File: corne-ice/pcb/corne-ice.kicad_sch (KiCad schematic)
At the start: 94 parts, among them J1 BAT, J2 nice!view, J3 BAT, J4 nice!view, SW1 SW_PUSH, SW10 SW_PUSH, SW11 SW_PUSH, SW12 SW_PUSH, SW13 SW_PUSH, SW14 SW_PUSH, SW15 SW_PUSH, SW16 SW_PUSH, SW17 SW_PUSH, SW18 SW_PUSH, SW19 SW_PUSH, SW2 SW_PUSH, SW20 SW_PUSH, SW21 SW_PUSH, SW22 SW_PUSH, SW23 SW_PUSH, SW24 SW_PUSH, SW25 SW_PUSH, SW26 SW_PUSH, SW27 SW_PUSH, SW28 SW_PUSH, SW29 SW_PUSH, SW3 SW_PUSH, SW30 SW_PUSH, SW31 SW_PUSH, SW32 SW_PUSH, SW33 SW_PUSH, SW34 SW_PUSH, SW35 SW_PUSH, SW36 SW_PUSH, SW37 SW_PUSH, SW38 SW_PUSH, SW39 SW_PUSH, SW4 SW_PUSH, SW40 SW_PUSH, SW41 SW_PUSH, SW42 SW_PUSH, SW5 SW_PUSH, SW6 SW_PUSH, SW7 SW_PUSH, SW8 SW_PUSH, SW9 SW_PUSH, U1 nice!nano, U2 nice!nano

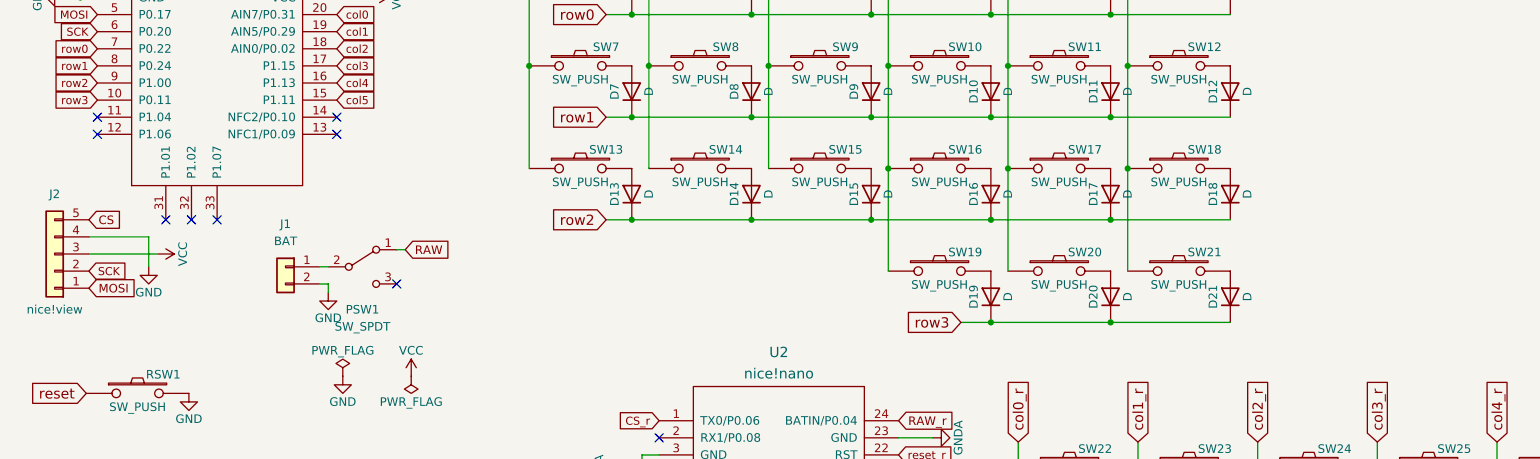
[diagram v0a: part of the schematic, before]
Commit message: Added a button and rotary encoder.
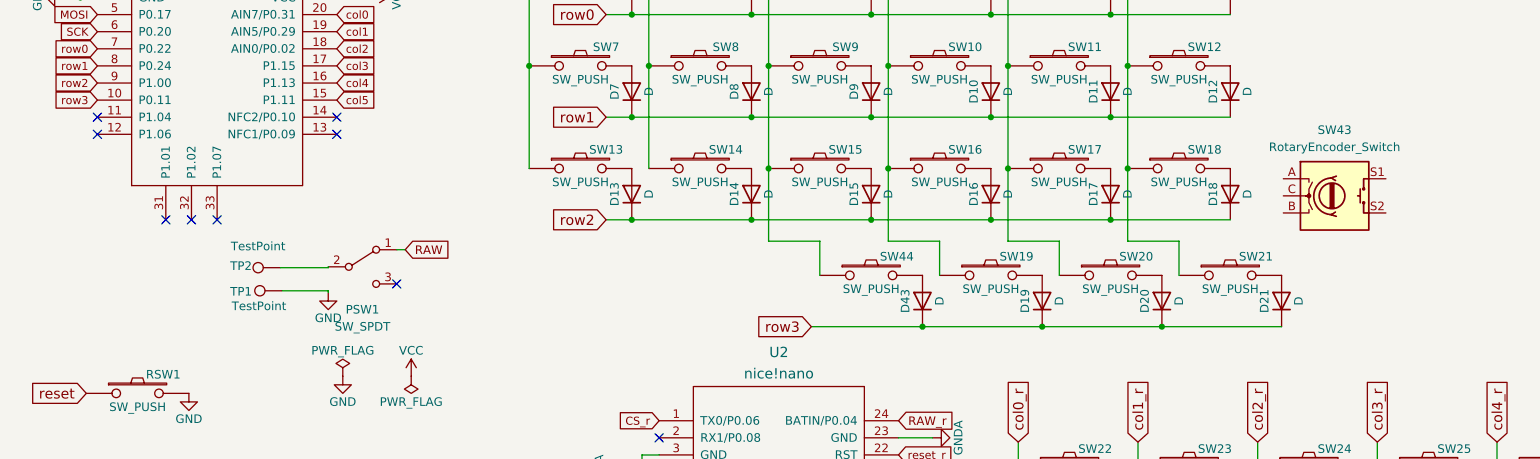
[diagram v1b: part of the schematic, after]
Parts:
- removed J1: BAT, Connector_JST:JST_PH_S2B-PH-SM4-TB_1x02-1MP_P2.00mm_Horizontal, symbol Connector_Generic:Conn_01x02
- removed J2: nice!view, Connector_PinHeader_2.54mm:PinHeader_1x05_P2.54mm_Vertical, symbol Connector_Generic:Conn_01x05
- added D43: D, kbd:D3_SMD_v2, symbol Device:D
- added SW43: RotaryEncoder_Switch, Rotary_Encoder:RotaryEncoder_Alps_EC11E-Switch_Vertical_H20mm, symbol Device:RotaryEncoder_Switch
- added SW44: SW_PUSH, kbd:CherryMX_Hotswap, symbol kbd:SW_PUSH
- added TP1: TestPoint, TestPoint:TestPoint_Pad_1.5x1.5mm, symbol Connector:TestPoint
- added TP2: TestPoint, TestPoint:TestPoint_Pad_D1.5mm, symbol Connector:TestPoint
- RSW1: footprint keeblib:alps_sksn -> Button_Switch_SMD:SW_Push_1P1T-MP_NO_Horizontal_Alps_SKRTLAE010
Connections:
- net GND: now also TP1.1
- net col2: now also SW44.1
- net row3: now also D43.1 (K)
- net at PSW1.2 (B): now also TP2.1
- new net: D43.2 (A), SW44.2
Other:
- moved on the sheet: D19, D20, D21, SW19, SW20, SW21
